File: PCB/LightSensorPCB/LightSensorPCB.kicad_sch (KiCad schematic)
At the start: 15 parts, among them J1 POWER/I2C, U1 LTR-329ALS-01, U2 LSM6DSMTR, U3 VL53L3CXV0DH/1

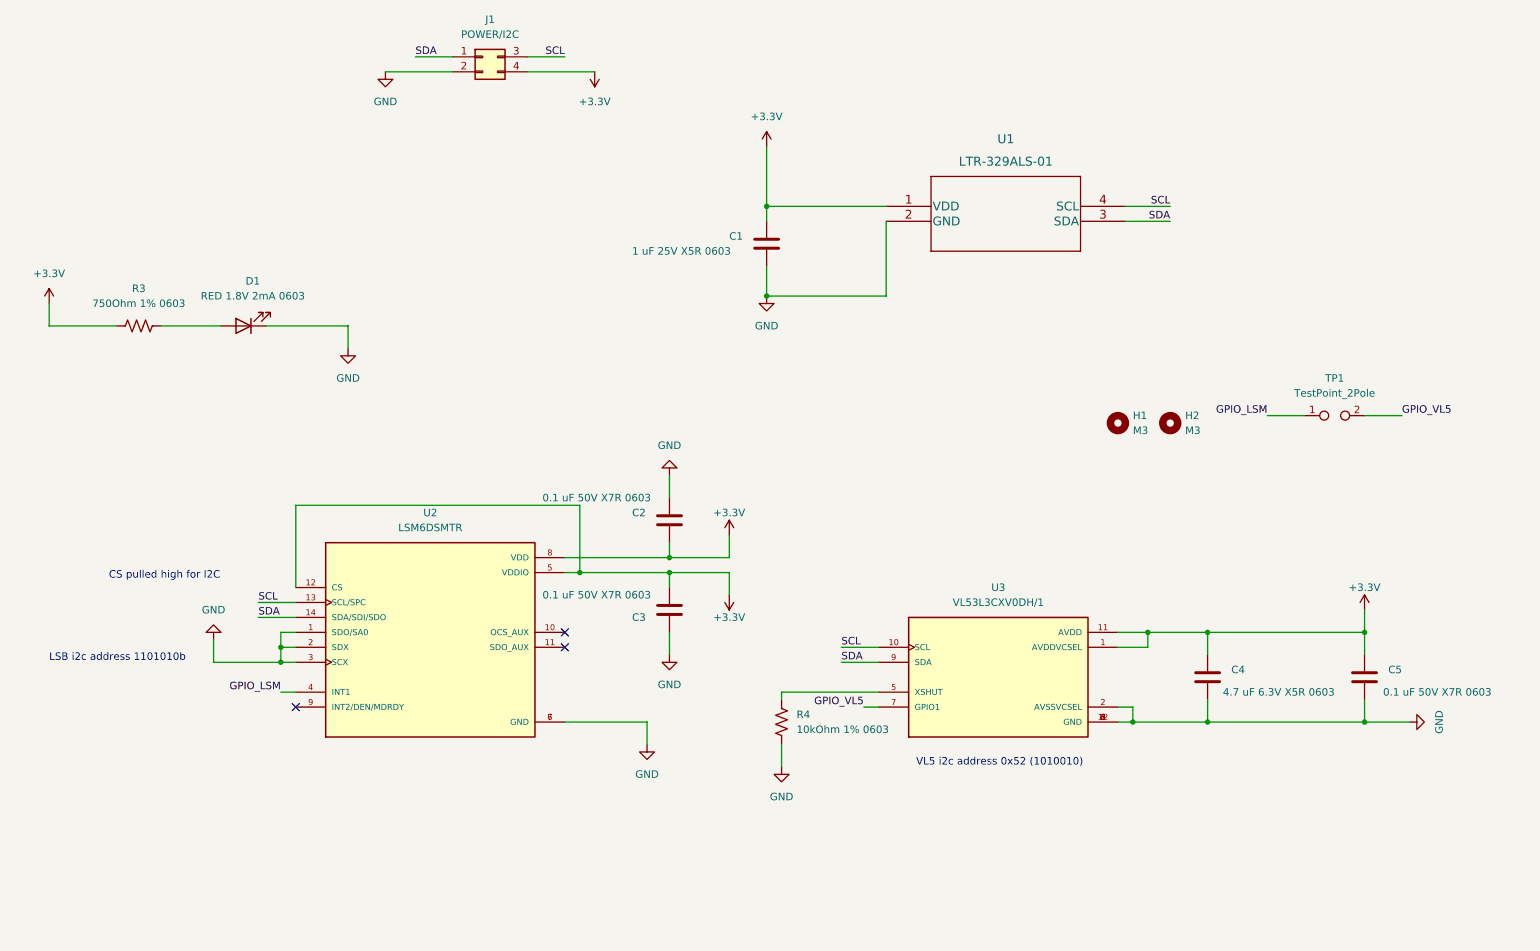
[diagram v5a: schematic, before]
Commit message: 3x PCB ready for gerberization
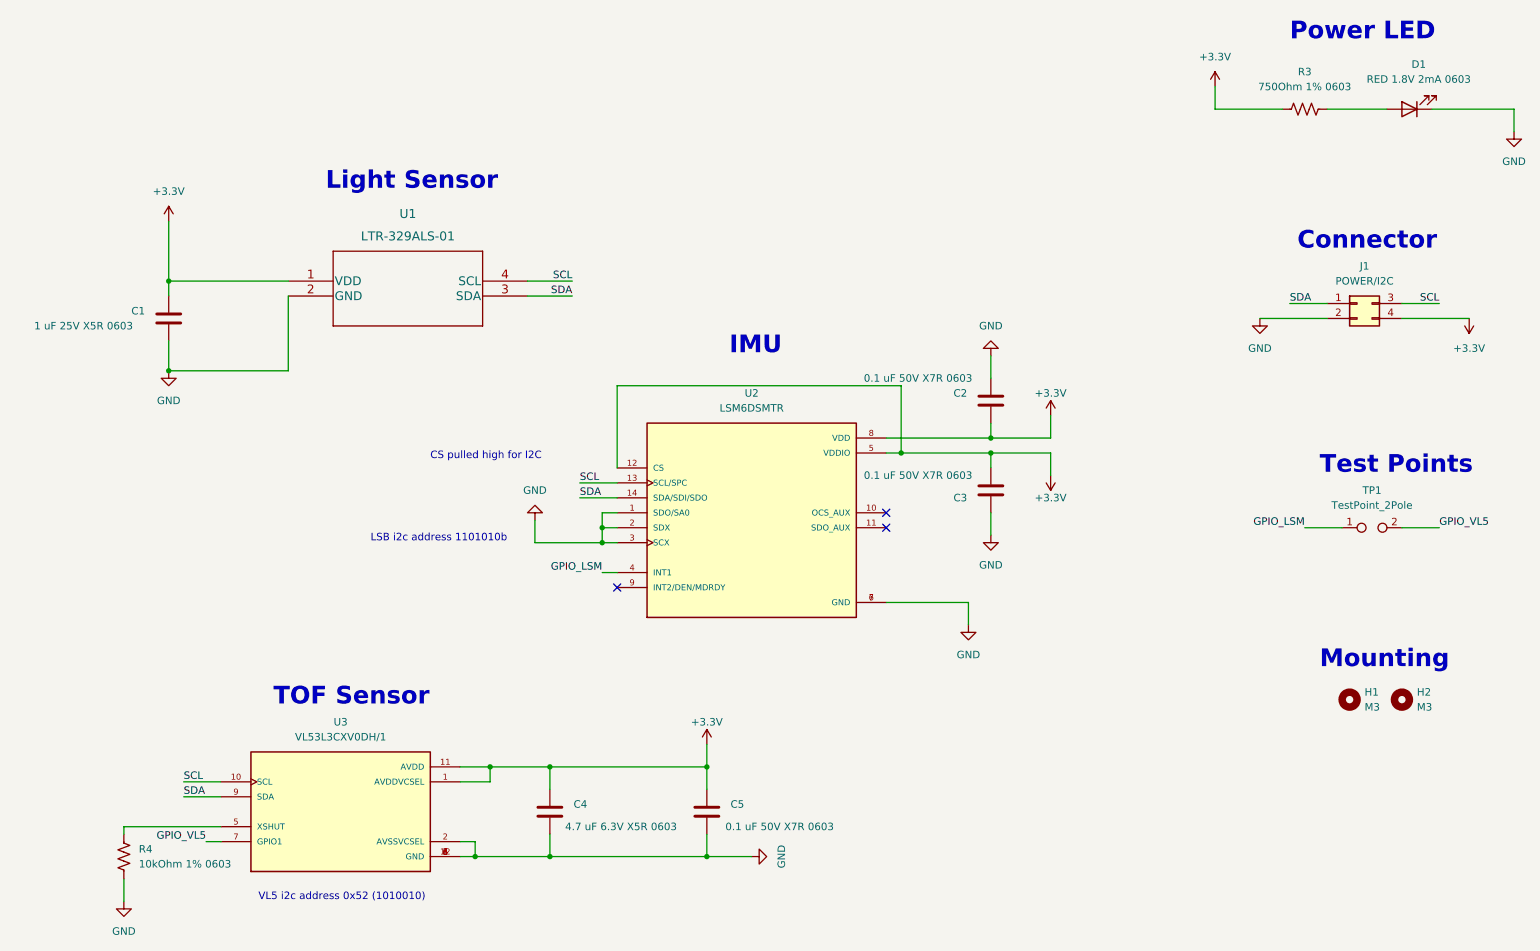
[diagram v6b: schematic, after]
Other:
- note added: "Connector"
- note added: "IMU"
- note added: "Light Sensor"
- note added: "Mounting"
- note added: "Power LED"
- note added: "TOF Sensor"
- note added: "Test Points"
- moved on the sheet: C1, C2, C3, C4, C5, D1, H1, H2, J1, R3, R4, TP1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

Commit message: 3x PCB ordered
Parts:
- C4: value 4.7 uF 6.3V X5R 0603 -> 4.7 uF 25V X5R 0805; footprint Capacitor_SMD:C_0603_1608Metric -> Capacitor_SMD:C_0805_2012Metric; Manufacturer Part Number CL10A475KQ8NNNC -> CL21A475KAQNNNE; Vendor Part Number 1276-1045-1-ND -> 1276-1244-1-ND
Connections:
- net +3.3V: now also R4.2
- net GND: no longer R4.1
- net at U3.5 (XSHUT): now also R4.1; no longer R4.2
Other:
- moved on the sheet: R4
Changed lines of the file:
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@@
-    (stroke (width 0) (type default) (color 0 0 0 0))
-  )
-  (wire (pts (xy 31.75 163.83) (xy 31.75 165.1))
     (stroke (width 0) (type default) (color 0 0 0 0))
   )
@@
     (stroke (width 0) (type default) (color 0 0 0 0))
   )
-  (wire (pts (xy 31.75 172.72) (xy 31.75 176.53))
-    (stroke (width 0) (type default) (color 0 0 0 0))
-  )
   (wire (pts (xy 248.92 113.03) (xy 255.27 113.03))
     (stroke (width 0) (type default) (color 0 0 0 0))
@@
   )
   (wire (pts (xy 91.44 166.37) (xy 91.44 168.91))
+    (stroke (width 0) (type default) (color 0 0 0 0))
+  )
+  (wire (pts (xy 31.75 162.56) (xy 31.75 163.83))
     (stroke (width 0) (type default) (color 0 0 0 0))
   )
@@
       (effects (font (size 1.27 1.27)) hide)
     )
-  )
-  (symbol (lib_id "power:GND") (at 31.75 176.53 0) (unit 1)
-    (in_bom yes) (on_board yes) (fields_autoplaced)
-    (property "Reference" "#PWR0115" (id 0) (at 31.75 182.88 0)
-      (effects (font (size 1.27 1.27)) hide)
-    )
-    (property "Value" "GND" (id 1) (at 31.75 181.61 0))
-    (property "Footprint" "" (id 2) (at 31.75 176.53 0)
-      (effects (font (size 1.27 1.27)) hide)
-    )
-    (property "Datasheet" "" (id 3) (at 31.75 176.53 0)
-      (effects (font (size 1.27 1.27)) hide)
-    )
-    (pin "1")
   )
   (symbol (lib_id "power:GND") (at 175.26 129.54 0) (unit 1)
@@
     (pin "9")
   )
+  (symbol (lib_id "power:+3.3V") (at 31.75 154.94 0) (mirror y) (unit 1)
+    (in_bom yes) (on_board yes)
+    (property "Reference" "#PWR0105" (id 0) (at 31.75 158.75 0)
+      (effects (font (size 1.27 1.27)) hide)
+    )
+    (property "Value" "+3.3V" (id 1) (at 31.75 151.13 0))
+    (property "Footprint" "" (id 2) (at 31.75 154.94 0)
+      (effects (font (size 1.27 1.27)) hide)
+    )
+    (property "Datasheet" "" (id 3) (at 31.75 154.94 0)
+      (effects (font (size 1.27 1.27)) hide)
+    )
+    (pin "1")
+  )
   (symbol (lib_id "Device:LED") (at 250.19 41.91 180) (unit 1)
     (in_bom yes) (on_board yes) (fields_autoplaced)
@@
     (pin "1")
   )
-  (symbol (lib_id "Device:R_US") (at 31.75 168.91 180) (unit 1)
-    (in_bom yes) (on_board yes) (fields_autoplaced)
-    (property "Reference" "R4" (id 0) (at 34.29 167.6399 0)
+  (symbol (lib_id "Device:R_US") (at 31.75 158.75 180) (unit 1)
+    (in_bom yes) (on_board yes)
+    (property "Reference" "R4" (id 0) (at 27.305 157.48 0)
       (effects (font (size 1.27 1.27)) (justify right))
     )
-    (property "Value" "10kOhm 1% 0603" (id 1) (at 34.29 170.1799 0)
+    (property "Value" "10kOhm 1% 0603" (id 1) (at 12.7 160.02 0)
       (effects (font (size 1.27 1.27)) (justify right))
     )
-    (property "Footprint" "Resistor_SMD:R_0603_1608Metric" (id 2) (at 30.734 168.656 90)
-      (effects (font (size 1.27 1.27)) hide)
-    )
-    (property "Datasheet" "~" (id 3) (at 31.75 168.91 0)
-      (effects (font (size 1.27 1.27)) hide)
-    )
-    (property "Manufacturer" "Stackpole Electronics Inc" (id 4) (at 31.75 168.91 0)
-      (effects (font (size 1.27 1.27)) hide)
-    )
-    (property "Manufacturer Part Number" "RNCP0603FTD10K0" (id 5) (at 31.75 168.91 0)
-      (effects (font (size 1.27 1.27)) hide)
-    )
-    (property "Vendor" "Digikey" (id 6) (at 31.75 168.91 0)
-      (effects (font (size 1.27 1.27)) hide)
-    )
-    (property "Vendor Part Number" "RNCP0603FTD10K0CT-ND" (id 7) (at 31.75 168.91 0)
+    (property "Footprint" "Resistor_SMD:R_0603_1608Metric" (id 2) (at 30.734 158.496 90)
+      (effects (font (size 1.27 1.27)) hide)
+    )
+    (property "Datasheet" "~" (id 3) (at 31.75 158.75 0)
+      (effects (font (size 1.27 1.27)) hide)
+    )
+    (property "Manufacturer" "Stackpole Electronics Inc" (id 4) (at 31.75 158.75 0)
+      (effects (font (size 1.27 1.27)) hide)
+    )
+    (property "Manufacturer Part Number" "RNCP0603FTD10K0" (id 5) (at 31.75 158.75 0)
+      (effects (font (size 1.27 1.27)) hide)
+    )
+    (property "Vendor" "Digikey" (id 6) (at 31.75 158.75 0)
+      (effects (font (size 1.27 1.27)) hide)
+    )
+    (property "Vendor Part Number" "RNCP0603FTD10K0CT-ND" (id 7) (at 31.75 158.75 0)
       (effects (font (size 1.27 1.27)) hide)
     )
@@
       (effects (font (size 1.27 1.27)) (justify left))
     )
-    (property "Value" "4.7 uF 6.3V X5R 0603" (id 1) (at 125.73 163.83 0)
-      (effects (font (size 1.27 1.27)) (justify left))
-    )
-    (property "Footprint" "Capacitor_SMD:C_0603_1608Metric" (id 2) (at 103.1748 165.1 0)
+    (property "Value" "4.7 uF 25V X5R 0805" (id 1) (at 125.73 163.83 0)
+      (effects (font (size 1.27 1.27)) (justify left))
+    )
+    (property "Footprint" "Capacitor_SMD:C_0805_2012Metric" (id 2) (at 103.1748 165.1 0)
       (effects (font (size 1.27 1.27)) hide)
     )
@@
       (effects (font (size 1.27 1.27)) hide)
     )
-    (property "Manufacturer Part Number" "CL10A475KQ8NNNC" (id 5) (at 104.14 161.29 0)
+    (property "Manufacturer Part Number" "CL21A475KAQNNNE" (id 5) (at 104.14 161.29 0)
       (effects (font (size 1.27 1.27)) hide)
     )
@@
       (effects (font (size 1.27 1.27)) hide)
     )
-    (property "Vendor Part Number" "1276-1045-1-ND" (id 7) (at 104.14 161.29 0)
+    (property "Vendor Part Number" "1276-1244-1-ND" (id 7) (at 104.14 161.29 0)
       (effects (font (size 1.27 1.27)) hide)
     )
@@
       (reference "#PWR0104") (unit 1) (value "+3.3V") (footprint "")
     )
+    (path "/3f480239-3dfb-4684-b51f-dca49b7a856e"
+      (reference "#PWR0105") (unit 1) (value "+3.3V") (footprint "")
+    )
     (path "/8064ce56-be3e-4761-96c0-c52b6787a81a"
       (reference "#PWR0106") (unit 1) (value "+3.3V") (footprint "")
@@
       (reference "#PWR0114") (unit 1) (value "GND") (footprint "")
     )
-    (path "/25b7e008-2f8b-423e-8322-0e179c9d7505"
-      (reference "#PWR0115") (unit 1) (value "GND") (footprint "")
-    )
     (path "/d39a68e4-135c-40ea-95f0-89c6f0a1bced"
       (reference "#PWR0116") (unit 1) (value "+3.3V") (footprint "")
@@
     )
     (path "/d21cb784-69ba-469b-83d7-4d574e498c6c"
-      (reference "C4") (unit 1) (value "4.7 uF 6.3V X5R 0603") (footprint "Capacitor_SMD:C_0603_1608Metric")
+      (reference "C4") (unit 1) (value "4.7 uF 25V X5R 0805") (footprint "Capacitor_SMD:C_0805_2012Metric")
     )
     (path "/4ced17c5-5460-4de9-bc5f-00a87f96b786"
